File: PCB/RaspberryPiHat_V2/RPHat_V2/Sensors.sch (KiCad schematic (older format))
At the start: 19 parts

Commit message: Schematic clean-up
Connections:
- net GNDREF: now also U?.1 (A1), U?.2 (A0)
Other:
- note added: "Slave address: 1000000"
- moved on the sheet: R?, U?
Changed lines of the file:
@@
 encoding utf-8
 Sheet 2 4
-Title ""
-Date ""
-Rev ""
+Title "Sensor subcircuits"
+Date "2021-05-15"
+Rev "0.1"
 Comp ""
 Comment1 ""
@@
 L RPHat_V2-rescue:GY-NEO6MV2-User_Created U?
 U 1 1 60929062
-P 10400 1350
-F 0 "U?" H 10778 1388 50  0000 L CNN
-F 1 "GY-NEO6MV2" H 10778 1297 50  0000 L CNN
-F 2 "Connector_PinHeader_2.54mm:PinHeader_1x04_P2.54mm_Vertical" H 10400 1700 50  0001 C CNN
-F 3 "" H 10400 1800 50  0001 C CNN
-	1    10400 1350
-	1    0    0    -1
-$EndComp
-Text GLabel 10300 1800 3    50   Input ~ 0
+P 9500 1800
+F 0 "U?" H 9878 1838 50  0000 L CNN
+F 1 "GY-NEO6MV2" H 9878 1747 50  0000 L CNN
+F 2 "Connector_PinHeader_2.54mm:PinHeader_1x04_P2.54mm_Vertical" H 9500 2150 50  0001 C CNN
+F 3 "" H 9500 2250 50  0001 C CNN
+	1    9500 1800
+	1    0    0    -1
+$EndComp
+Text GLabel 9400 2250 3    50   Input ~ 0
 GPS_RX
-Text GLabel 10500 1800 3    50   Input ~ 0
+Text GLabel 9600 2250 3    50   Input ~ 0
 GPS_TX
 $Comp
 L power:GNDREF #PWR?
 U 1 1 6092ABE6
-P 10150 1800
-F 0 "#PWR?" H 10150 1550 50  0001 C CNN
-F 1 "GNDREF" H 10155 1627 50  0000 C CNN
-F 2 "" H 10150 1800 50  0001 C CNN
-F 3 "" H 10150 1800 50  0001 C CNN
-	1    10150 1800
+P 9250 2250
+F 0 "#PWR?" H 9250 2000 50  0001 C CNN
+F 1 "GNDREF" H 9255 2077 50  0001 C CNN
+F 2 "" H 9250 2250 50  0001 C CNN
+F 3 "" H 9250 2250 50  0001 C CNN
+	1    9250 2250
 	1    0    0    -1
 $EndComp
@@
 L power:+5V #PWR?
 U 1 1 6092B06D
-P 10650 1800
-F 0 "#PWR?" H 10650 1650 50  0001 C CNN
-F 1 "+5V" H 10665 1973 50  0000 C CNN
-F 2 "" H 10650 1800 50  0001 C CNN
-F 3 "" H 10650 1800 50  0001 C CNN
-	1    10650 1800
+P 9750 2250
+F 0 "#PWR?" H 9750 2100 50  0001 C CNN
+F 1 "+5V" H 9765 2423 50  0000 C CNN
+F 2 "" H 9750 2250 50  0001 C CNN
+F 3 "" H 9750 2250 50  0001 C CNN
+	1    9750 2250
 	-1   0    0    1
 $EndComp
 Wire Wire Line
-	10150 1650 10150 1800
-Wire Wire Line
-	10300 1650 10300 1800
-Wire Wire Line
-	10500 1650 10500 1800
-Wire Wire Line
-	10650 1650 10650 1800
-Text GLabel 6150 1550 0    50   Input ~ 0
+	9250 2100 9250 2250
+Wire Wire Line
+	9400 2100 9400 2250
+Wire Wire Line
+	9600 2100 9600 2250
+Wire Wire Line
+	9750 2100 9750 2250
+Text GLabel 6350 1550 0    50   Input ~ 0
 SPI_MISO_18
-Text GLabel 6150 1650 0    50   Input ~ 0
+Text GLabel 6350 1650 0    50   Input ~ 0
 SPI_MOSI_18
-Text GLabel 6150 1750 0    50   Input ~ 0
+Text GLabel 6350 1750 0    50   Input ~ 0
 SPI_CLK_18
-Text GLabel 6150 1850 0    50   Input ~ 0
+Text GLabel 6350 1850 0    50   Input ~ 0
 IMU_CS_18
-Wire Wire Line
-	6150 1550 6450 1550
-Wire Wire Line
-	6150 1650 6450 1650
-Wire Wire Line
-	6150 1750 6450 1750
-Wire Wire Line
-	6150 1850 6450 1850
 $Comp
 L power:+1V8 #PWR?
@@
 Wire Wire Line
 	6850 1100 6850 1150
-Text GLabel 5500 2300 0    50   Input ~ 0
+Text GLabel 5550 2150 0    50   Input ~ 0
 IMU_INT_18
 $Comp
@@
 P 6950 2800
 F 0 "#PWR?" H 6950 2550 50  0001 C CNN
-F 1 "GNDREF" H 6955 2627 50  0000 C CNN
+F 1 "GNDREF" H 6955 2627 50  0001 C CNN
 F 2 "" H 6950 2800 50  0001 C CNN
 F 3 "" H 6950 2800 50  0001 C CNN
@@
 Wire Wire Line
 	6950 2550 6950 2800
-Text GLabel 3050 1400 2    50   Input ~ 0
+Text GLabel 2950 1400 2    50   Input ~ 0
 SPI_MISO_18
-Text GLabel 3050 1800 2    50   Input ~ 0
+Text GLabel 2950 1800 2    50   Input ~ 0
 SPI_MOSI_18
-Text GLabel 3050 1600 2    50   Input ~ 0
+Text GLabel 2950 1600 2    50   Input ~ 0
 SPI_CLK_18
-Wire Wire Line
-	2900 1400 3050 1400
-Wire Wire Line
-	2900 1600 3050 1600
-Wire Wire Line
-	2900 1800 3050 1800
 $Comp
 L power:GNDREF #PWR?
@@
 P 2300 2450
 F 0 "#PWR?" H 2300 2200 50  0001 C CNN
-F 1 "GNDREF" H 2305 2277 50  0000 C CNN
+F 1 "GNDREF" H 2305 2277 50  0001 C CNN
 F 2 "" H 2300 2450 50  0001 C CNN
 F 3 "" H 2300 2450 50  0001 C CNN
@@
 L Device:R R?
 U 1 1 6093CA08
-P 3650 1850
-F 0 "R?" H 3720 1896 50  0000 L CNN
-F 1 "100k" H 3720 1805 50  0000 L CNN
-F 2 "Resistor_SMD:R_0603_1608Metric_Pad0.98x0.95mm_HandSolder" V 3580 1850 50  0001 C CNN
-F 3 "~" H 3650 1850 50  0001 C CNN
-	1    3650 1850
+P 3600 1800
+F 0 "R?" H 3670 1846 50  0000 L CNN
+F 1 "100k" H 3670 1755 50  0000 L CNN
+F 2 "Resistor_SMD:R_0603_1608Metric_Pad0.98x0.95mm_HandSolder" V 3530 1800 50  0001 C CNN
+F 3 "~" H 3600 1800 50  0001 C CNN
+	1    3600 1800
 	1    0    0    -1
 $EndComp
@@
 L power:+1V8 #PWR?
 U 1 1 6093DA5A
-P 3650 1600
-F 0 "#PWR?" H 3650 1450 50  0001 C CNN
-F 1 "+1V8" H 3665 1773 50  0000 C CNN
-F 2 "" H 3650 1600 50  0001 C CNN
-F 3 "" H 3650 1600 50  0001 C CNN
-	1    3650 1600
-	1    0    0    -1
-$EndComp
-Wire Wire Line
-	3650 1600 3650 1700
-Connection ~ 3650 2000
-Wire Wire Line
-	3650 2000 3750 2000
+P 3600 1600
+F 0 "#PWR?" H 3600 1450 50  0001 C CNN
+F 1 "+1V8" H 3615 1773 50  0000 C CNN
+F 2 "" H 3600 1600 50  0001 C CNN
+F 3 "" H 3600 1600 50  0001 C CNN
+	1    3600 1600
+	1    0    0    -1
+$EndComp
 $Comp
 L Device:R R?
 U 1 1 609401EF
-P 5550 2000
-F 0 "R?" H 5620 2046 50  0000 L CNN
-F 1 "100k" H 5620 1955 50  0000 L CNN
-F 2 "Resistor_SMD:R_0603_1608Metric_Pad0.98x0.95mm_HandSolder" V 5480 2000 50  0001 C CNN
-F 3 "~" H 5550 2000 50  0001 C CNN
-	1    5550 2000
+P 5700 1950
+F 0 "R?" H 5770 1996 50  0000 L CNN
+F 1 "100k" H 5770 1905 50  0000 L CNN
+F 2 "Resistor_SMD:R_0603_1608Metric_Pad0.98x0.95mm_HandSolder" V 5630 1950 50  0001 C CNN
+F 3 "~" H 5700 1950 50  0001 C CNN
+	1    5700 1950
 	1    0    0    -1
 $EndComp
@@
 L power:+1V8 #PWR?
 U 1 1 609401F5
-P 5450 1750
-F 0 "#PWR?" H 5450 1600 50  0001 C CNN
-F 1 "+1V8" H 5465 1923 50  0000 C CNN
-F 2 "" H 5450 1750 50  0001 C CNN
-F 3 "" H 5450 1750 50  0001 C CNN
-	1    5450 1750
-	1    0    0    -1
-$EndComp
-Wire Wire Line
-	5550 1750 5550 1850
-Wire Wire Line
-	5550 2150 6450 2150
+P 5700 1750
+F 0 "#PWR?" H 5700 1600 50  0001 C CNN
+F 1 "+1V8" H 5715 1923 50  0000 C CNN
+F 2 "" H 5700 1750 50  0001 C CNN
+F 3 "" H 5700 1750 50  0001 C CNN
+	1    5700 1750
+	1    0    0    -1
+$EndComp
+Wire Wire Line
+	5700 1750 5700 1800
 $Comp
 L Device:C C?
@@
 $EndComp
 Wire Wire Line
-	1500 1600 1500 2400
-Wire Wire Line
-	1500 2400 2200 2400
-Connection ~ 2200 2400
-Wire Wire Line
 	2200 1050 1500 1050
 Wire Wire Line
@@
 	1050 1050 1050 1300
 Connection ~ 1500 1050
-Wire Wire Line
-	1050 1600 1050 2400
-Wire Wire Line
-	1050 2400 1500 2400
-Connection ~ 1500 2400
 $Comp
 L Device:C C?
@@
 P 1200 3650
 F 0 "#PWR?" H 1200 3400 50  0001 C CNN
-F 1 "GNDREF" V 1205 3522 50  0000 R CNN
+F 1 "GNDREF" V 1205 3522 50  0001 R CNN
 F 2 "" H 1200 3650 50  0001 C CNN
 F 3 "" H 1200 3650 50  0001 C CNN
@@
 P 1300 4400
 F 0 "#PWR?" H 1300 4150 50  0001 C CNN
-F 1 "GNDREF" V 1305 4272 50  0000 R CNN
+F 1 "GNDREF" V 1305 4272 50  0001 R CNN
 F 2 "" H 1300 4400 50  0001 C CNN
 F 3 "" H 1300 4400 50  0001 C CNN
@@
 Text GLabel 1250 3750 2    50   Input ~ 0
 HE_R_OUTPUT
-Wire Wire Line
-	5500 2300 5550 2300
-Wire Wire Line
-	5550 2300 5550 2150
-Connection ~ 5550 2150
-Wire Wire Line
-	5550 1750 5450 1750
-Wire Wire Line
-	2900 2000 3650 2000
 $Comp
 L RPHat_V2-rescue:TXB0108YZPR2-TXB0108YZPR2 IC?
@@
 	3350 6200 3550 6200
 Wire Wire Line
-	4000 6450 4000 6550
+	4000 6450 4000 6500
 $Comp
 L power:+BATT #PWR?
@@
 Wire Wire Line
 	2700 6250 2700 6400
+Wire Wire Line
+	4400 6150 4550 6150
+Wire Wire Line
+	4550 6500 4000 6500
+Wire Wire Line
+	4550 6150 4550 6250
+Connection ~ 4000 6500
+Wire Wire Line
+	4000 6500 4000 6550
+Wire Wire Line
+	4400 6250 4550 6250
+Connection ~ 4550 6250
+Wire Wire Line
+	4550 6250 4550 6500
+Text Notes 3650 6750 0    50   ~ 0
+Slave address: 1000000
+Wire Wire Line
+	6350 1550 6450 1550
+Wire Wire Line
+	6350 1650 6450 1650
+Wire Wire Line
+	6350 1750 6450 1750
+Wire Wire Line
+	6350 1850 6450 1850
+Wire Wire Line
+	5550 2150 5700 2150
+Wire Wire Line
+	5700 2100 5700 2150
+Connection ~ 5700 2150
+Wire Wire Line
+	5700 2150 6450 2150
+Wire Wire Line
+	2950 1400 2900 1400
+Wire Wire Line
+	2950 1600 2900 1600
+Wire Wire Line
+	2950 1800 2900 1800
+Wire Wire Line
+	2900 2000 3600 2000
+Wire Wire Line
+	3600 1950 3600 2000
+Connection ~ 3600 2000
+Wire Wire Line
+	3600 2000 3750 2000
+Wire Wire Line
+	3600 1600 3600 1650
+$Comp
+L power:GNDREF #PWR?
+U 1 1 60B79349
+P 1300 1650
+F 0 "#PWR?" H 1300 1400 50  0001 C CNN
+F 1 "GNDREF" H 1305 1477 50  0001 C CNN
+F 2 "" H 1300 1650 50  0001 C CNN
+F 3 "" H 1300 1650 50  0001 C CNN
+	1    1300 1650
+	1    0    0    -1
+$EndComp
+Wire Wire Line
+	1500 1600 1500 1650
+Wire Wire Line
+	1500 1650 1300 1650
+Wire Wire Line
+	1050 1600 1050 1650
+Wire Wire Line
+	1050 1650 1300 1650
+Connection ~ 1300 1650
 $EndSCHEMATC

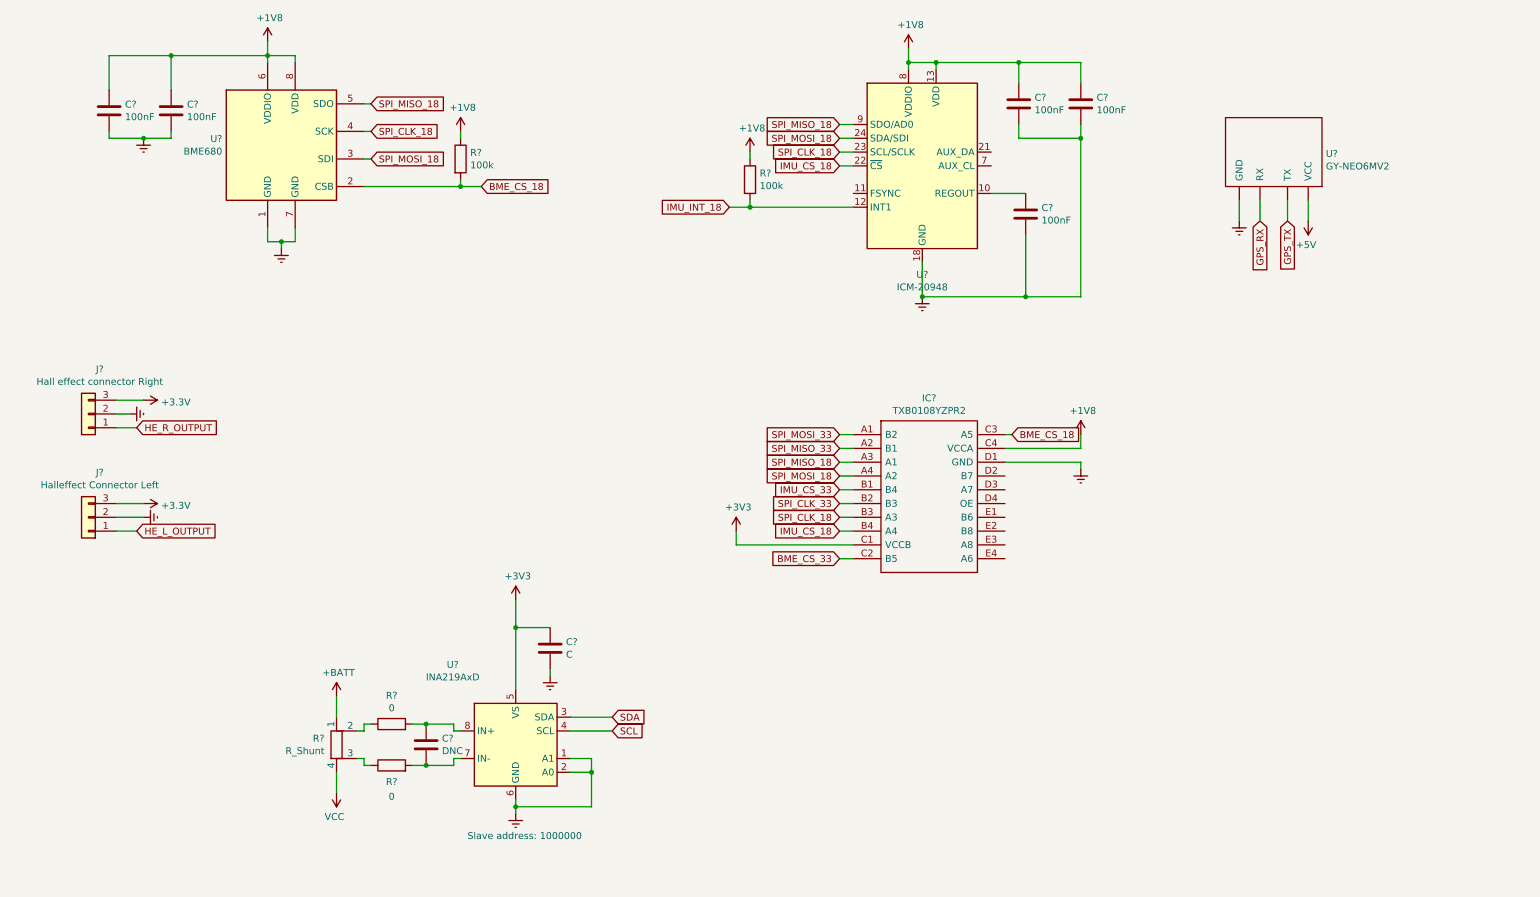
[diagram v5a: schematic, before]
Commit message: Started routing PCB
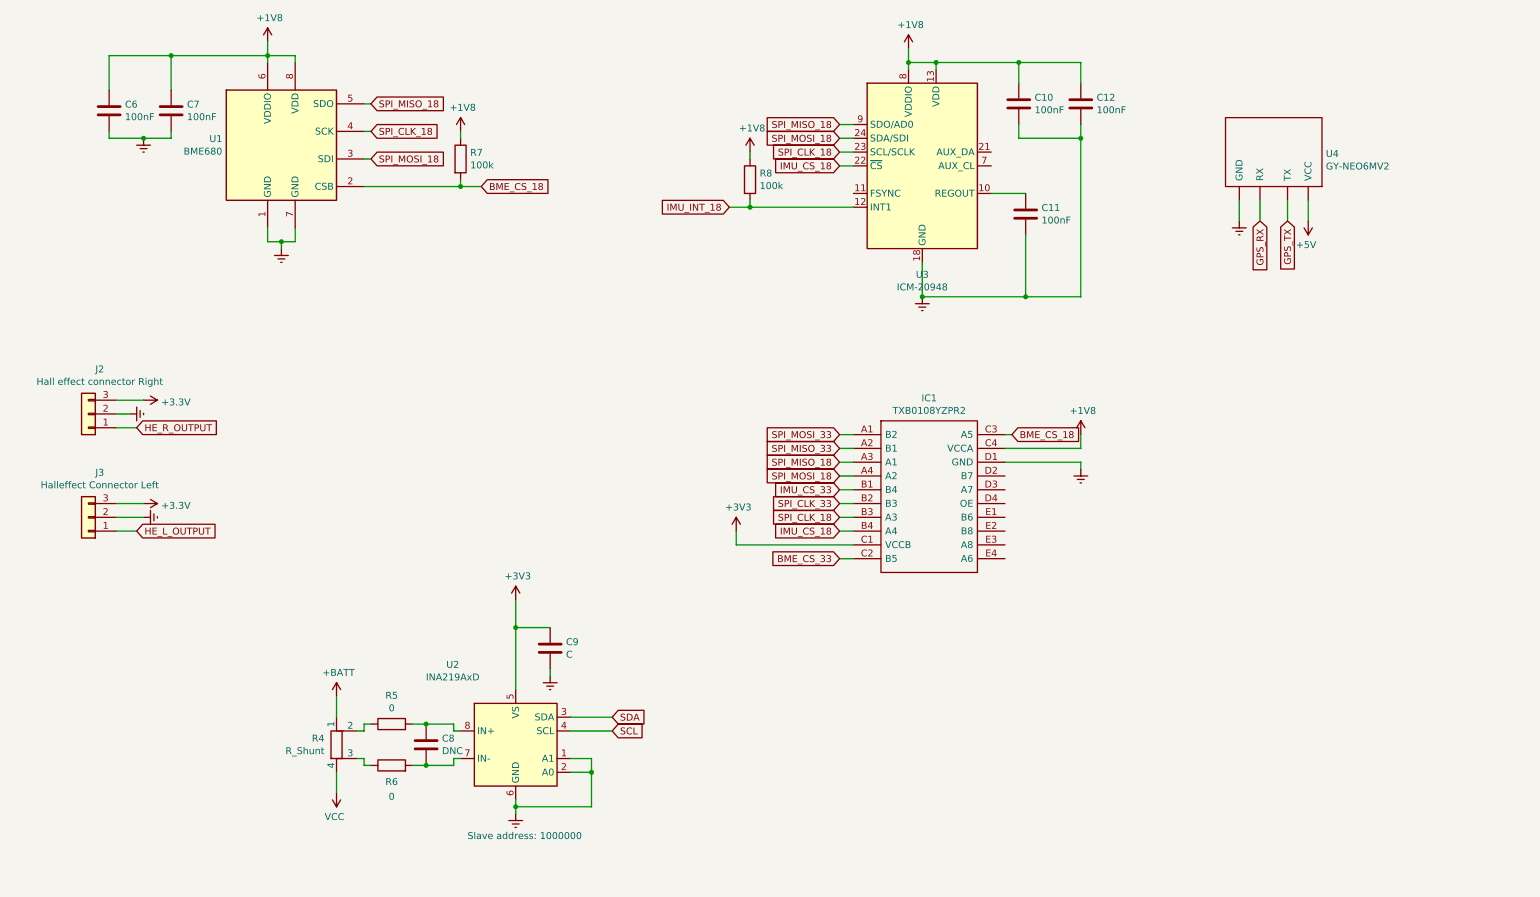
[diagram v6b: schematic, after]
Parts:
- gave numbers to parts that had none: 19
